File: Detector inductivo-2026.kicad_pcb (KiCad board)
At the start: 2 copper layers, 90.5 x 16.2 mm, 21 parts, among them Q1 2N2222A, Q2 BC557, Q3 BC557, Q4 2N2222A

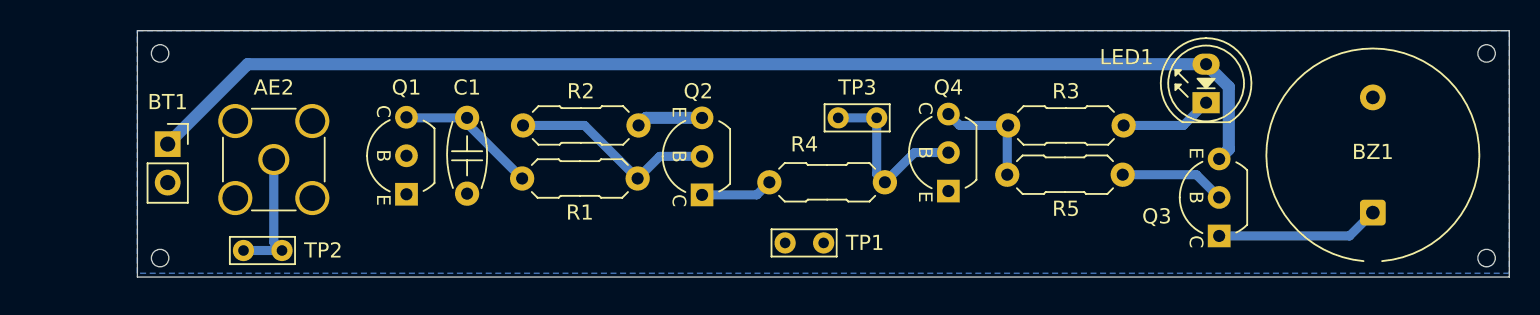
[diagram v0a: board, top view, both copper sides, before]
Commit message: cambios en el terminal de 9V
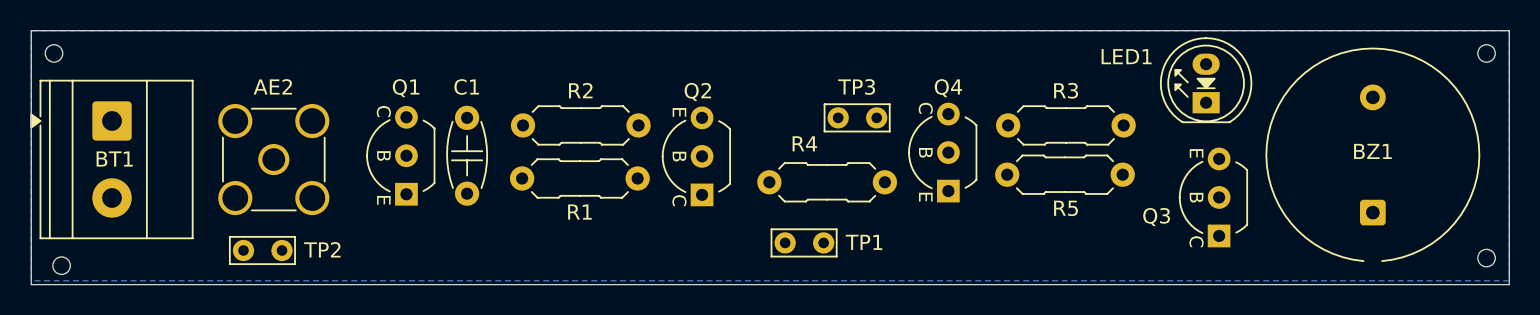
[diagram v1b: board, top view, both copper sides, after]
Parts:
- BT1: footprint Connector_PinSocket_2.54mm:PinSocket_1x02_P2.54mm_Vertical -> TerminalBlock_Phoenix:TerminalBlock_Phoenix_MKDS-1,5-2-5.08_1x02_P5.08mm_Horizontal
- moved H1 7.00 mm to (99.5, 92.0)
- moved H2 6.52 mm to (100.0, 106.0)
- moved BT1 3.98 mm to (103.3, 96.5), turned to -90 degrees
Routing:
- net /9V: track 82.2 -> 0.00 mm
- net Net-(Q2-B): track 13.9 -> 0.00 mm
- net Net-(Q4-B): track 12.0 -> 0.00 mm
- net Net-(BZ1-+): track 10.8 -> 0.00 mm
- net Net-(Q1-C): track 9.87 -> 0.00 mm
- net Net-(AE2-A): track 8.76 -> 0.00 mm
- net Net-(Q4-C): track 7.53 -> 0.00 mm
- net Net-(Q3-B): track 6.98 -> 0.00 mm
- net Net-(LED1-K): track 6.06 -> 0.00 mm
- net Net-(Q2-C): track 4.78 -> 0.00 mm
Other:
- board size 90.5 x 16.2 mm -> 97.5 x 16.8 mm

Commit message: ruteo manual
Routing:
- net /9V: track 0.00 -> 83.6 mm
- net Net-(AE2-A): track 0.00 -> 17.6 mm
- net Net-(Q2-B): track 0.00 -> 13.9 mm
- net Net-(Q4-B): track 0.00 -> 12.0 mm
- net Net-(BZ1-+): track 0.00 -> 10.8 mm
- net Net-(Q1-C): track 0.00 -> 9.52 mm
- net Net-(Q4-C): track 0.00 -> 7.53 mm
- net Net-(Q3-B): track 0.00 -> 6.98 mm
- net Net-(LED1-K): track 0.00 -> 6.06 mm
- net Net-(Q2-C): track 0.00 -> 4.78 mm
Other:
- board size 97.5 x 16.8 mm -> 98 x 16.8 mm

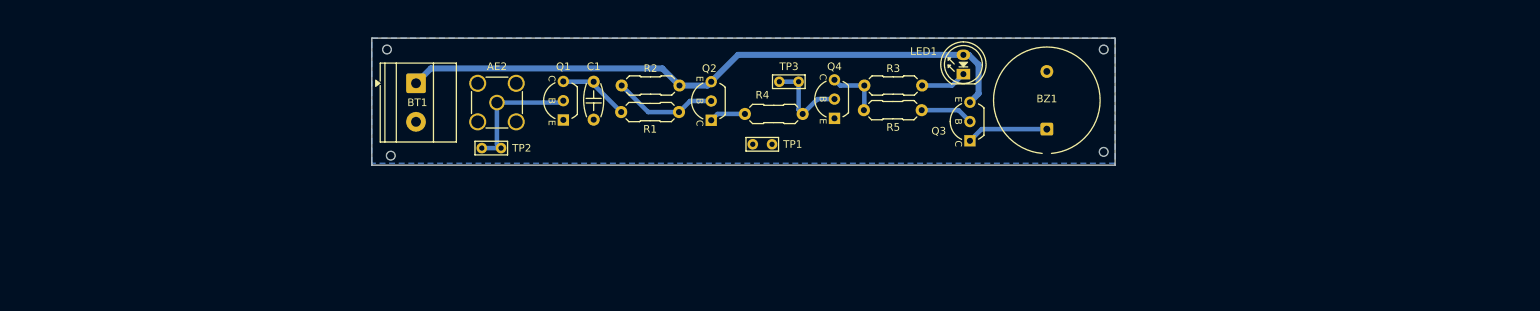
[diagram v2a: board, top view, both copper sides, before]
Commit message: Hice una matriz de 2x2 y generé el pdf para imprimir
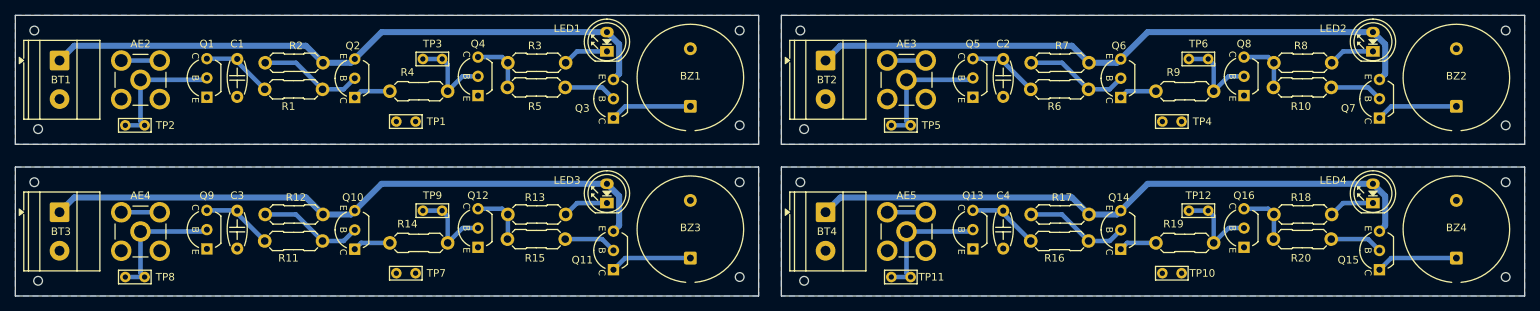
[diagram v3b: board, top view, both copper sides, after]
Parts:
- added AE2: Antenna_Shield, Conector_sma:SMA_Amphenol_132134-11_Vertical, F.Cu at (67.0, 96.0)
- added AE3: Antenna_Shield, Conector_sma:SMA_Amphenol_132134-11_Vertical, F.Cu at (168.0, 96.0)
- added AE4: Antenna_Shield, Conector_sma:SMA_Amphenol_132134-11_Vertical, F.Cu at (67.0, 116.0)
- added BT1: Battery, TerminalBlock_Phoenix:TerminalBlock_Phoenix_MKDS-1,5-2-5.08_1x02_P5.08mm_Horizontal, F.Cu at (56.3, 93.5)
- added BT2: Battery, TerminalBlock_Phoenix:TerminalBlock_Phoenix_MKDS-1,5-2-5.08_1x02_P5.08mm_Horizontal, F.Cu at (157.3, 93.5)
- added BT3: Battery, TerminalBlock_Phoenix:TerminalBlock_Phoenix_MKDS-1,5-2-5.08_1x02_P5.08mm_Horizontal, F.Cu at (56.3, 113.5)
- added BZ1: Buzzer, Buzzer_Beeper:Indicator_PUI_AI-1440-TWT-24V-2-R, F.Cu at (139.5, 99.5)
- added BZ2: Buzzer, Buzzer_Beeper:Indicator_PUI_AI-1440-TWT-24V-2-R, F.Cu at (240.5, 99.5)
- added BZ3: Buzzer, Buzzer_Beeper:Indicator_PUI_AI-1440-TWT-24V-2-R, F.Cu at (139.5, 119.5)
- added C1: 100nF, PCM_Capacitor_THT_AKL:C_Disc_D4.7mm_W2.5mm_P5.00mm, F.Cu at (79.8, 93.2)
- added C2: 100nF, PCM_Capacitor_THT_AKL:C_Disc_D4.7mm_W2.5mm_P5.00mm, F.Cu at (180.8, 93.2)
- added C3: 100nF, PCM_Capacitor_THT_AKL:C_Disc_D4.7mm_W2.5mm_P5.00mm, F.Cu at (79.8, 113.2)
- added H1: MountingHole, MountingHole:ToolingHole_1.152mm, F.Cu at (53.0, 89.5)
- added H10: MountingHole, MountingHole:ToolingHole_1.152mm, F.Cu at (53.5, 122.5)
- added H11: MountingHole, MountingHole:ToolingHole_1.152mm, F.Cu at (146.0, 122.0)
- added H12: MountingHole, MountingHole:ToolingHole_1.152mm, F.Cu at (146.0, 109.5)
- added H2: MountingHole, MountingHole:ToolingHole_1.152mm, F.Cu at (53.5, 102.5)
- added H3: MountingHole, MountingHole:ToolingHole_1.152mm, F.Cu at (146.0, 102.0)
- added H4: MountingHole, MountingHole:ToolingHole_1.152mm, F.Cu at (146.0, 89.5)
- added H5: MountingHole, MountingHole:ToolingHole_1.152mm, F.Cu at (154.0, 89.5)
- added H6: MountingHole, MountingHole:ToolingHole_1.152mm, F.Cu at (154.5, 102.5)
- added H7: MountingHole, MountingHole:ToolingHole_1.152mm, F.Cu at (247.0, 102.0)
- added H8: MountingHole, MountingHole:ToolingHole_1.152mm, F.Cu at (247.0, 89.5)
- added H9: MountingHole, MountingHole:ToolingHole_1.152mm, F.Cu at (53.0, 109.5)
- added LED1: LED_5mm_Green, PCM_LED_THT_AKL:LED_D5.0mm, F.Cu at (128.5, 92.2)
- added LED2: LED_5mm_Green, PCM_LED_THT_AKL:LED_D5.0mm, F.Cu at (229.5, 92.2)
- added LED3: LED_5mm_Green, PCM_LED_THT_AKL:LED_D5.0mm, F.Cu at (128.5, 112.2)
- added Q1: 2N2222A, PCM_Package_TO_SOT_THT_AKL:TO-92_Inline_Wide_EBC, F.Cu at (75.8, 98.3)
- added Q10: BC557, PCM_Package_TO_SOT_THT_AKL:TO-92_Inline_Wide_CBE, F.Cu at (95.2, 118.3)
- added Q11: BC557, PCM_Package_TO_SOT_THT_AKL:TO-92_Inline_Wide_CBE, F.Cu at (129.4, 121.0)
- added Q12: 2N2222A, PCM_Package_TO_SOT_THT_AKL:TO-92_Inline_Wide_EBC, F.Cu at (111.5, 118.1)
- added Q2: BC557, PCM_Package_TO_SOT_THT_AKL:TO-92_Inline_Wide_CBE, F.Cu at (95.2, 98.3)
- added Q3: BC557, PCM_Package_TO_SOT_THT_AKL:TO-92_Inline_Wide_CBE, F.Cu at (129.4, 101.0)
- added Q4: 2N2222A, PCM_Package_TO_SOT_THT_AKL:TO-92_Inline_Wide_EBC, F.Cu at (111.5, 98.1)
- added Q5: 2N2222A, PCM_Package_TO_SOT_THT_AKL:TO-92_Inline_Wide_EBC, F.Cu at (176.8, 98.3)
- added Q6: BC557, PCM_Package_TO_SOT_THT_AKL:TO-92_Inline_Wide_CBE, F.Cu at (196.2, 98.3)
- added Q7: BC557, PCM_Package_TO_SOT_THT_AKL:TO-92_Inline_Wide_CBE, F.Cu at (230.4, 101.0)
- added Q8: 2N2222A, PCM_Package_TO_SOT_THT_AKL:TO-92_Inline_Wide_EBC, F.Cu at (212.5, 98.1)
- added Q9: 2N2222A, PCM_Package_TO_SOT_THT_AKL:TO-92_Inline_Wide_EBC, F.Cu at (75.8, 118.3)
- added R1: 100k, Resistencias:R_Axial_DIN0207_L6.3mm_D2.5mm_P7.62mm_Horizontal, F.Cu at (83.4, 97.2)
- added R10: 10k, Resistencias:R_Axial_DIN0207_L6.3mm_D2.5mm_P7.62mm_Horizontal, F.Cu at (216.4, 97.0)
- added R11: 100k, Resistencias:R_Axial_DIN0207_L6.3mm_D2.5mm_P7.62mm_Horizontal, F.Cu at (83.4, 117.2)
- added R12: 1M, Resistencias:R_Axial_DIN0207_L6.3mm_D2.5mm_P7.62mm_Horizontal, F.Cu at (91.1, 113.8)
- added R13: 47, Resistencias:R_Axial_DIN0207_L6.3mm_D2.5mm_P7.62mm_Horizontal, F.Cu at (123.1, 113.8)
- added R14: 100k, Resistencias:R_Axial_DIN0207_L6.3mm_D2.5mm_P7.62mm_Horizontal, F.Cu at (99.9, 117.5)
- added R15: 10k, Resistencias:R_Axial_DIN0207_L6.3mm_D2.5mm_P7.62mm_Horizontal, F.Cu at (115.4, 117.0)
- added R19: 100k, Resistencias:R_Axial_DIN0207_L6.3mm_D2.5mm_P7.62mm_Horizontal, F.Cu at (200.9, 117.5)
- added R2: 1M, Resistencias:R_Axial_DIN0207_L6.3mm_D2.5mm_P7.62mm_Horizontal, F.Cu at (91.1, 93.8)
- added R3: 47, Resistencias:R_Axial_DIN0207_L6.3mm_D2.5mm_P7.62mm_Horizontal, F.Cu at (123.1, 93.8)
- added R5: 10k, Resistencias:R_Axial_DIN0207_L6.3mm_D2.5mm_P7.62mm_Horizontal, F.Cu at (115.4, 97.0)
- added R6: 100k, Resistencias:R_Axial_DIN0207_L6.3mm_D2.5mm_P7.62mm_Horizontal, F.Cu at (184.4, 97.2)
- added R7: 1M, Resistencias:R_Axial_DIN0207_L6.3mm_D2.5mm_P7.62mm_Horizontal, F.Cu at (192.1, 93.8)
- added R8: 47, Resistencias:R_Axial_DIN0207_L6.3mm_D2.5mm_P7.62mm_Horizontal, F.Cu at (224.1, 93.8)
- added R9: 100k, Resistencias:R_Axial_DIN0207_L6.3mm_D2.5mm_P7.62mm_Horizontal, F.Cu at (200.9, 97.5)
- added TP1: TestPoint_Probe, TestPoint:TestPoint_Bridge_Pitch2.54mm_Drill0.7mm, F.Cu at (100.7, 101.5)
- added TP2: TestPoint_Probe, TestPoint:TestPoint_Bridge_Pitch2.54mm_Drill0.7mm, F.Cu at (65.0, 102.0)
- added TP3: TestPoint_Probe, TestPoint:TestPoint_Bridge_Pitch2.54mm_Drill0.7mm, F.Cu at (104.2, 93.2)
- added TP4: TestPoint_Probe, TestPoint:TestPoint_Bridge_Pitch2.54mm_Drill0.7mm, F.Cu at (201.7, 101.5)
- added TP5: TestPoint_Probe, TestPoint:TestPoint_Bridge_Pitch2.54mm_Drill0.7mm, F.Cu at (166.0, 102.0)
- added TP6: TestPoint_Probe, TestPoint:TestPoint_Bridge_Pitch2.54mm_Drill0.7mm, F.Cu at (205.2, 93.2)
- added TP7: TestPoint_Probe, TestPoint:TestPoint_Bridge_Pitch2.54mm_Drill0.7mm, F.Cu at (100.7, 121.5)
- added TP8: TestPoint_Probe, TestPoint:TestPoint_Bridge_Pitch2.54mm_Drill0.7mm, F.Cu at (65.0, 122.0)
- added TP9: TestPoint_Probe, TestPoint:TestPoint_Bridge_Pitch2.54mm_Drill0.7mm, F.Cu at (104.2, 113.2)
- AE5: renamed from AE2; footprint Connector_Coaxial:SMA_Amphenol_132134-11_Vertical -> Conector_sma:SMA_Amphenol_132134-11_Vertical
- R16: renamed from R1; footprint PCM_Resistor_THT_AKL:R_Axial_DIN0207_L6.3mm_D2.5mm_P7.62mm_Horizontal -> Resistencias:R_Axial_DIN0207_L6.3mm_D2.5mm_P7.62mm_Horizontal
- R17: renamed from R2; footprint PCM_Resistor_THT_AKL:R_Axial_DIN0207_L6.3mm_D2.5mm_P7.62mm_Horizontal -> Resistencias:R_Axial_DIN0207_L6.3mm_D2.5mm_P7.62mm_Horizontal
- R18: renamed from R3; footprint PCM_Resistor_THT_AKL:R_Axial_DIN0207_L6.3mm_D2.5mm_P7.62mm_Horizontal -> Resistencias:R_Axial_DIN0207_L6.3mm_D2.5mm_P7.62mm_Horizontal
- R20: renamed from R5; footprint PCM_Resistor_THT_AKL:R_Axial_DIN0207_L6.3mm_D2.5mm_P7.62mm_Horizontal -> Resistencias:R_Axial_DIN0207_L6.3mm_D2.5mm_P7.62mm_Horizontal
- R4: footprint PCM_Resistor_THT_AKL:R_Axial_DIN0207_L6.3mm_D2.5mm_P7.62mm_Horizontal -> Resistencias:R_Axial_DIN0207_L6.3mm_D2.5mm_P7.62mm_Horizontal
- moved H13 57.2 mm to (154.0, 109.5)
- moved H14 56.9 mm to (154.5, 122.5)
- moved AE5 56.6 mm to (168.0, 116.0)
- moved BZ4 56.6 mm to (240.5, 119.5)
- moved C4 56.6 mm to (180.8, 113.2)
- moved LED4 56.6 mm to (229.5, 112.2)
- moved Q13 56.6 mm to (176.8, 118.3)
- moved Q14 56.6 mm to (196.2, 118.3)
- moved Q15 56.6 mm to (230.4, 121.0)
- moved Q16 56.6 mm to (212.5, 118.1)
- moved R16 56.6 mm to (184.4, 117.2)
- moved R17 56.6 mm to (192.1, 113.8)
- moved R18 56.6 mm to (224.1, 113.8)
- moved R20 56.6 mm to (216.4, 117.0)
- moved TP10 56.6 mm to (201.7, 121.5)
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- renumbered BT1 to BT4, BZ1 to BZ4, C1 to C4, H1 to H13, H2 to H14, H3 to H15, H4 to H16, LED1 to LED4, Q1 to Q13, Q2 to Q14, Q3 to Q15, Q4 to Q16, TP1 to TP10, TP2 to TP11, TP3 to TP12
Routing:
- net /9V: track 83.6 -> 331.2 mm
- net Net-(AE2-A): track 17.6 -> 70.5 mm
- net Net-(Q2-B): track 13.9 -> 55.5 mm
- net Net-(Q4-B): track 12.0 -> 47.6 mm
- net Net-(BZ1-+): track 10.8 -> 43.1 mm
- net Net-(Q1-C): track 9.52 -> 38.1 mm
- net Net-(Q4-C): track 7.53 -> 30.1 mm
- net Net-(Q3-B): track 6.98 -> 27.9 mm
- net GND: track 0.00 -> 20.3 mm
- net Net-(LED1-K): track 6.06 -> 24.2 mm
- net Net-(Q2-C): track 4.78 -> 19.9 mm
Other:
- board size 98 x 16.8 mm -> 199 x 37 mm
